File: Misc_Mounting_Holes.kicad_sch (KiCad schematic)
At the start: 15 parts

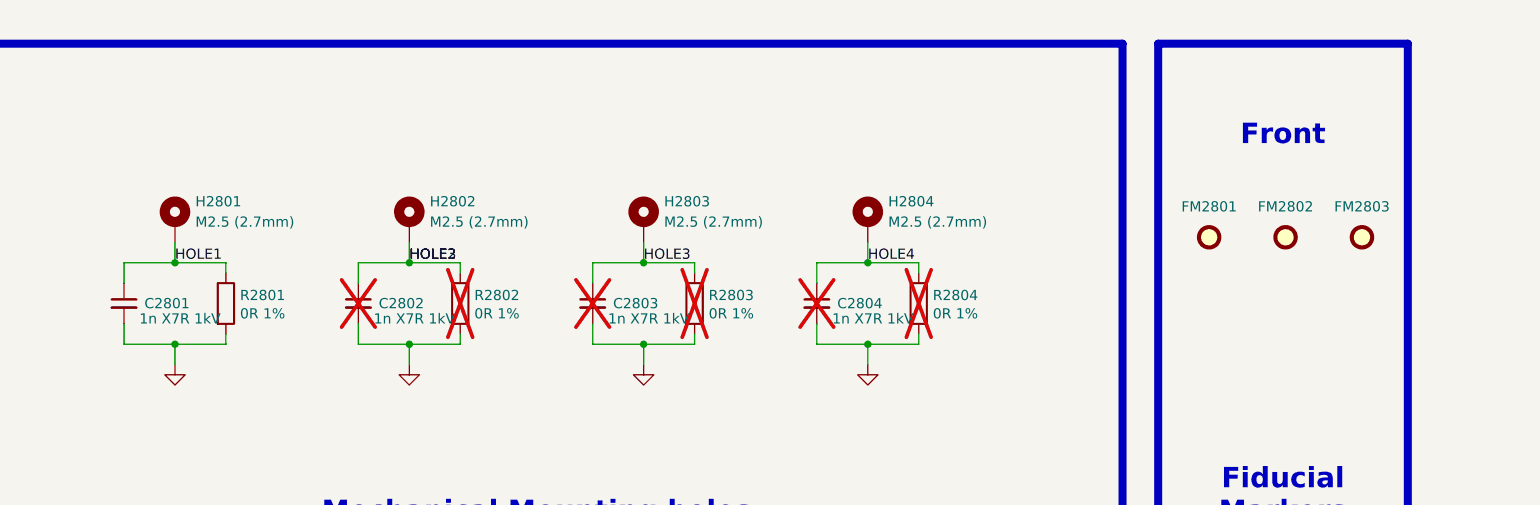
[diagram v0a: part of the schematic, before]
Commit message: Added RGB LED, added motor connectors, added test points, imported all 3D models
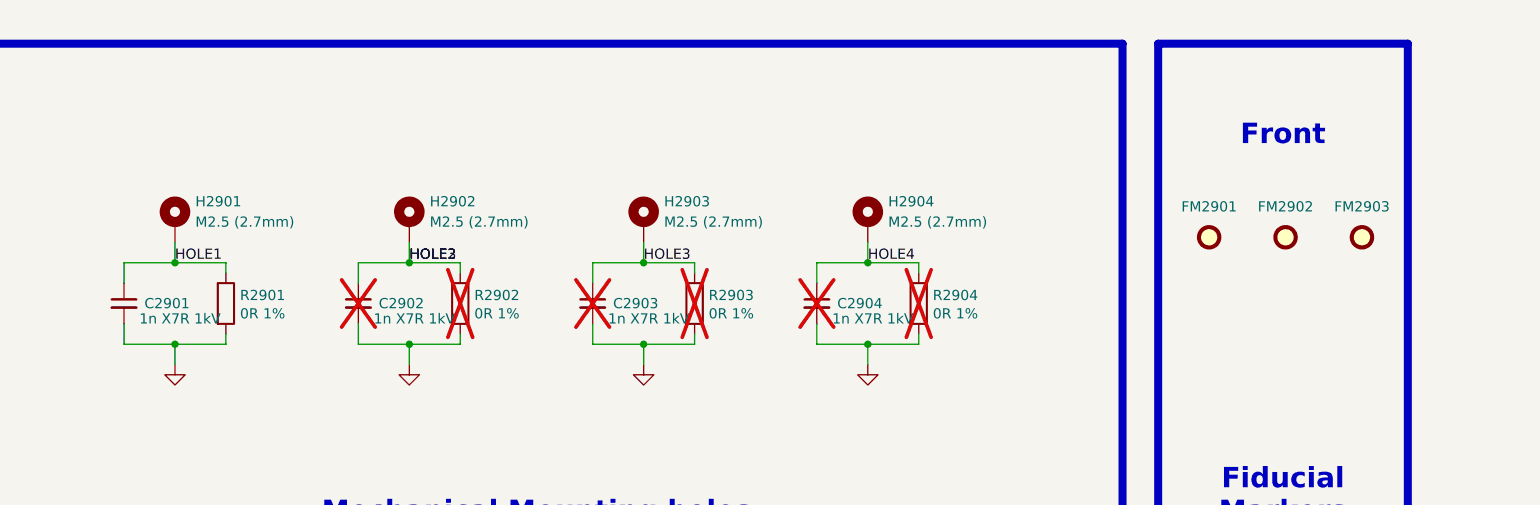
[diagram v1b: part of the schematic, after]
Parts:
- renumbered C2801 to C2901, C2802 to C2902, C2803 to C2903, C2804 to C2904, FM2801 to FM2901, FM2802 to FM2902, FM2803 to FM2903, H2801 to H2901, H2802 to H2902, H2803 to H2903, H2804 to H2904, R2801 to R2901, R2802 to R2902, R2803 to R2903, R2804 to R2904

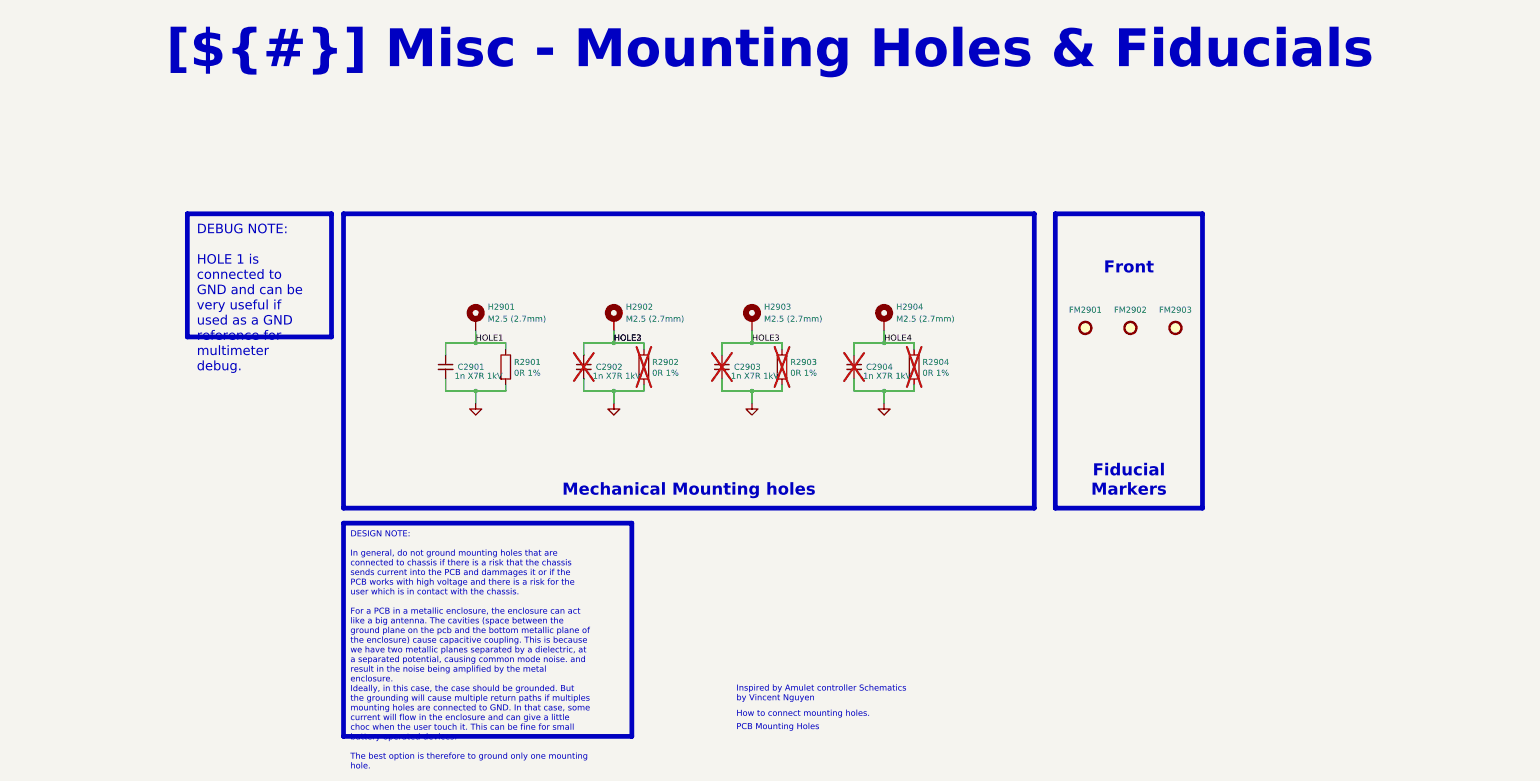
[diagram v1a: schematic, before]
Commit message: Finished schematic, imported all footprints, all 3D models and created STM32 project, now need to proofread shematic before layout
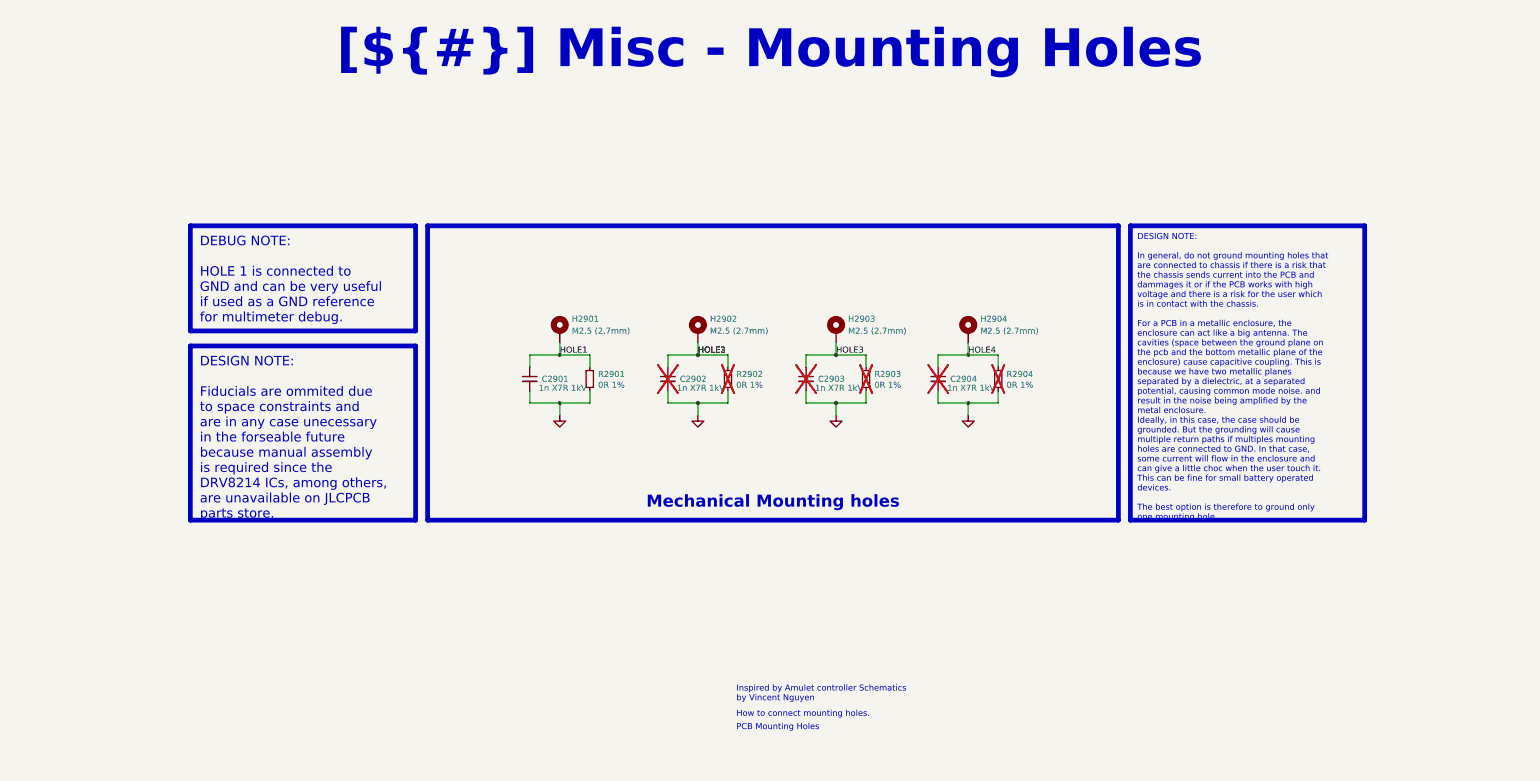
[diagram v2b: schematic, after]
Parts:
- removed FM2901, FM2902, FM2903: Fiducial, Charge_Manager_FP:Fiducial_1mm_Mask2mm, symbol Mechanical:Fiducial
- removed R2902, R2903, R2904: 0R 1%, Resistor_SMD:R_0603_1608Metric, symbol Device:R
- added R2902, R2903, R2904: 0R 1%, Resistor_SMD:R_0603_1608Metric, symbol Device:R_Small
- C2901, C2902, C2903, C2904: Manufacturer Part Number C0603C102MDRAC7081 -> C0603C102KDRACTU; Supplier Part Number 80-C0603C102MDRAC -> 80-C0603C102KDRACTU
- R2901: symbol Device:R -> Device:R_Small
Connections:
- net GND: now also R2902.2, R2903.2, R2904.2
- net HOLE2: now also R2902.1, R2903.1
- net HOLE4: now also R2904.1
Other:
- title: Misc - Mounting Holes & Fiducials -> Misc - Mounting Holes
- moved on the sheet: C2901, C2902, C2903, C2904, H2901, H2902, H2903, H2904, R2901

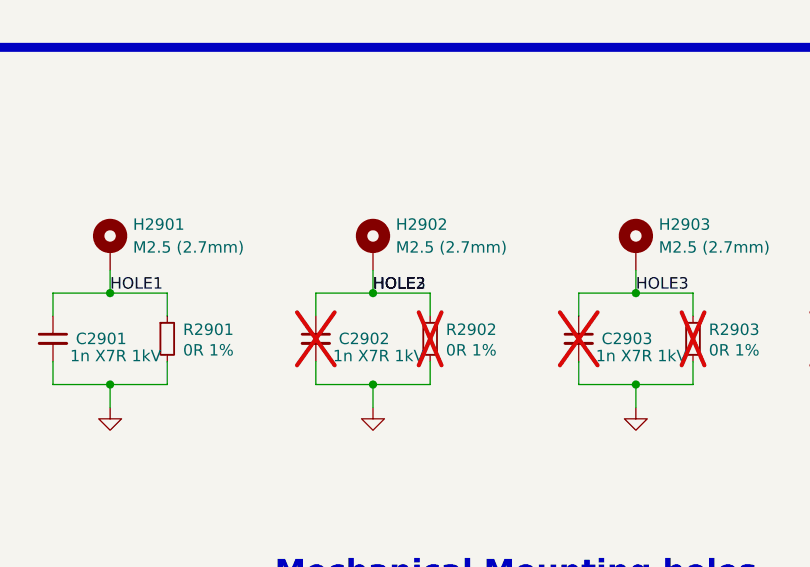
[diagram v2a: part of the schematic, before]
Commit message: Reviewed shematic, cleaned all DRC errors, chosed stackup, started layout
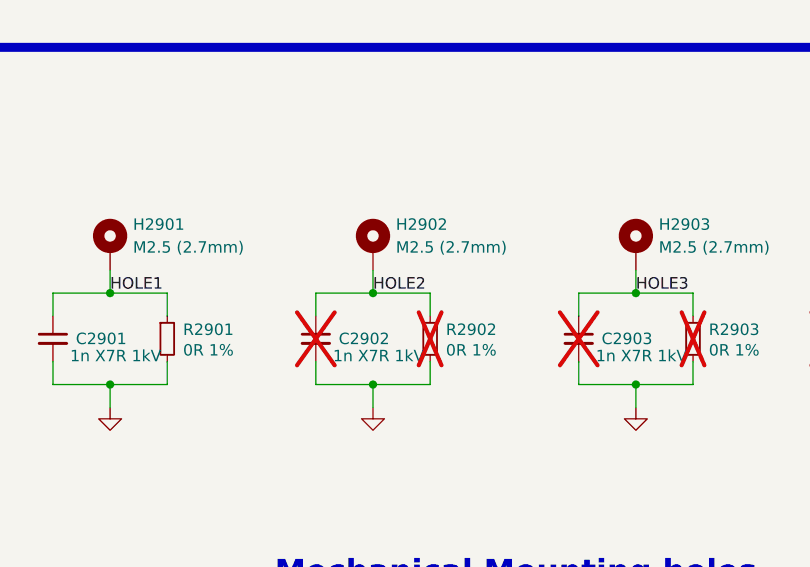
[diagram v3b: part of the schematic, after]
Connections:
- net HOLE2: no longer C2903.1, H2903.1, R2903.1
- new net HOLE3: C2903.1, H2903.1, R2903.1
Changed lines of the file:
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@@
-		)
-	)
-	(label "HOLE3"
-		(at 133.35 91.44 0)
-		(effects
-			(font
-				(size 1.27 1.27)
-			)
-			(justify left bottom)
 		)
 	)

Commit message: Finished layout, only cleaning left
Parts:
- C2901, R2901: now not fitted
- C2902, R2902: now fitted
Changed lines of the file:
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@@
 		(in_bom yes)
 		(on_board yes)
-		(dnp no)
+		(dnp yes)
 		(property "Reference" "C2901"
 			(at 100.33 96.52 0)
@@
 		(in_bom yes)
 		(on_board yes)
-		(dnp yes)
+		(dnp no)
 		(property "Reference" "R2902"
 			(at 144.272 95.504 0)
@@
 		(in_bom yes)
 		(on_board yes)
-		(dnp no)
+		(dnp yes)
 		(property "Reference" "R2901"
 			(at 115.062 95.504 0)
@@
 		(in_bom yes)
 		(on_board yes)
-		(dnp yes)
+		(dnp no)
 		(property "Reference" "C2902"
 			(at 129.54 96.52 0)

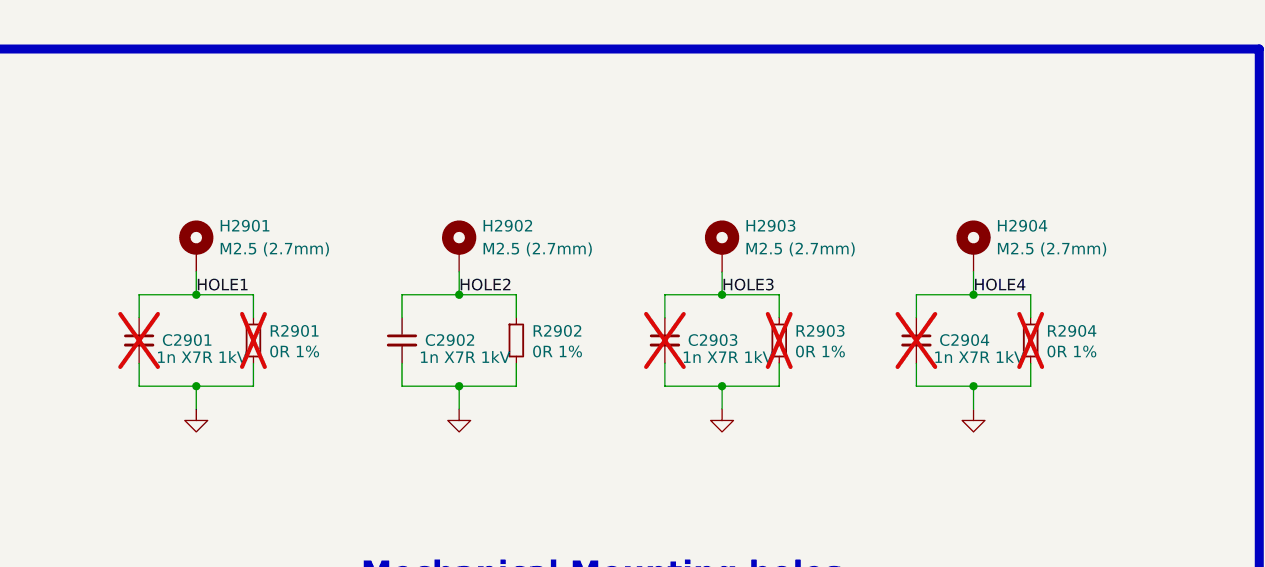
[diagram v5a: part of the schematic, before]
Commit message: Finished cleaning routing, removed errors, cleaned shematics, added pictures and other improvements
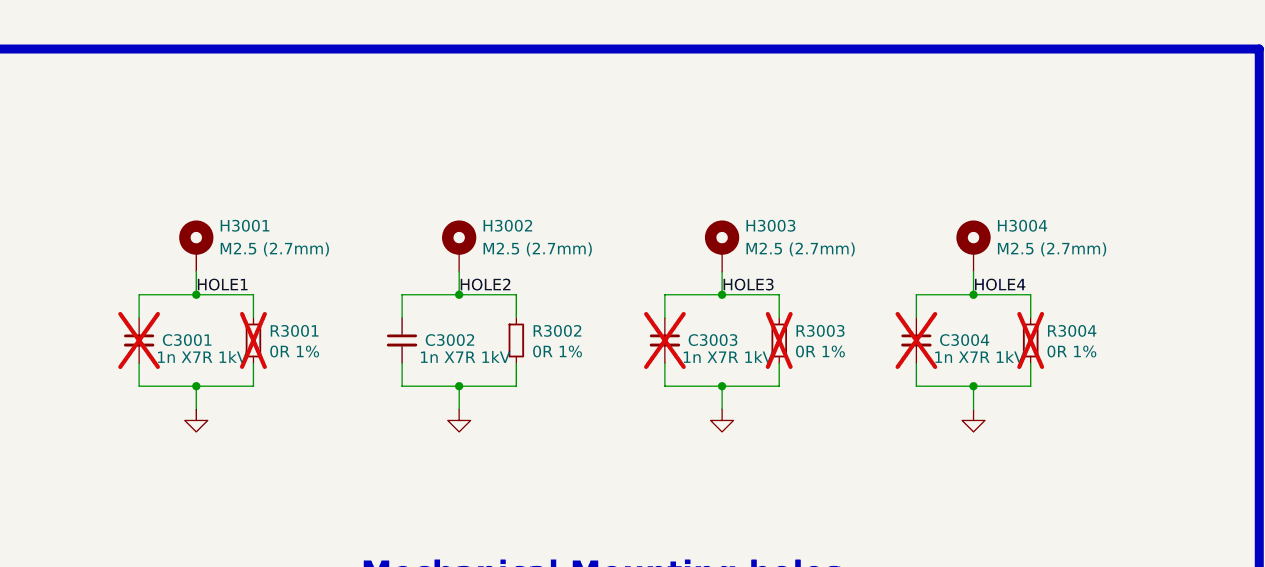
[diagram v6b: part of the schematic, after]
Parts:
- renumbered C2901 to C3001, C2902 to C3002, C2903 to C3003, C2904 to C3004, H2901 to H3001, H2902 to H3002, H2903 to H3003, H2904 to H3004, R2901 to R3001, R2902 to R3002, R2903 to R3003, R2904 to R3004
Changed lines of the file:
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@@
 		(on_board yes)
 		(dnp yes)
-		(property "Reference" "R2903"
+		(property "Reference" "R3003"
 			(at 173.482 95.504 0)
 			(effects
@@
 			(project "Plume"
 				(path "/0650c7a8-acba-429c-9f8e-eec0baf0bc1c/fede4c36-00cc-4d3d-b71c-5243ba232202/93c115ca-2823-4ddf-b830-32015e2ac9e9"
-					(reference "R2903")
+					(reference "R3003")
 					(unit 1)
 				)
@@
 		(on_board yes)
 		(dnp yes)
-		(property "Reference" "C2901"
+		(property "Reference" "C3001"
 			(at 100.33 96.52 0)
 			(effects
@@
 			(project "Plume"
 				(path "/0650c7a8-acba-429c-9f8e-eec0baf0bc1c/fede4c36-00cc-4d3d-b71c-5243ba232202/93c115ca-2823-4ddf-b830-32015e2ac9e9"
-					(reference "C2901")
+					(reference "C3001")
 					(unit 1)
 				)
@@
 		(on_board yes)
 		(dnp no)
-		(property "Reference" "R2902"
+		(property "Reference" "R3002"
 			(at 144.272 95.504 0)
 			(effects
@@
 			(project "Plume"
 				(path "/0650c7a8-acba-429c-9f8e-eec0baf0bc1c/fede4c36-00cc-4d3d-b71c-5243ba232202/93c115ca-2823-4ddf-b830-32015e2ac9e9"
-					(reference "R2902")
+					(reference "R3002")
 					(unit 1)
 				)
@@
 		(dnp no)
 		(fields_autoplaced yes)
-		(property "Reference" "H2901"
+		(property "Reference" "H3001"
 			(at 106.68 83.82 0)
 			(effects
@@
 			(project "Plume"
 				(path "/0650c7a8-acba-429c-9f8e-eec0baf0bc1c/fede4c36-00cc-4d3d-b71c-5243ba232202/93c115ca-2823-4ddf-b830-32015e2ac9e9"
-					(reference "H2901")
+					(reference "H3001")
 					(unit 1)
 				)
@@
 		(dnp no)
 		(fields_autoplaced yes)
-		(property "Reference" "H2902"
+		(property "Reference" "H3002"
 			(at 135.89 83.82 0)
 			(effects
@@
 			(project "Plume"
 				(path "/0650c7a8-acba-429c-9f8e-eec0baf0bc1c/fede4c36-00cc-4d3d-b71c-5243ba232202/93c115ca-2823-4ddf-b830-32015e2ac9e9"
-					(reference "H2902")
+					(reference "H3002")
 					(unit 1)
 				)
@@
 		(on_board yes)
 		(dnp yes)
-		(property "Reference" "C2904"
+		(property "Reference" "C3004"
 			(at 186.69 96.52 0)
 			(effects
@@
 			(project "Plume"
 				(path "/0650c7a8-acba-429c-9f8e-eec0baf0bc1c/fede4c36-00cc-4d3d-b71c-5243ba232202/93c115ca-2823-4ddf-b830-32015e2ac9e9"
-					(reference "C2904")
+					(reference "C3004")
 					(unit 1)
 				)
@@
 		(dnp no)
 		(fields_autoplaced yes)
-		(property "Reference" "H2903"
+		(property "Reference" "H3003"
 			(at 165.1 83.82 0)
 			(effects
@@
 			(project "Plume"
 				(path "/0650c7a8-acba-429c-9f8e-eec0baf0bc1c/fede4c36-00cc-4d3d-b71c-5243ba232202/93c115ca-2823-4ddf-b830-32015e2ac9e9"
-					(reference "H2903")
+					(reference "H3003")
 					(unit 1)
 				)
@@
 		(dnp no)
 		(fields_autoplaced yes)
-		(property "Reference" "#PWR02903"
+		(property "Reference" "#PWR03003"
 			(at 162.56 110.49 0)
 			(effects
@@
 			(project "Plume"
 				(path "/0650c7a8-acba-429c-9f8e-eec0baf0bc1c/fede4c36-00cc-4d3d-b71c-5243ba232202/93c115ca-2823-4ddf-b830-32015e2ac9e9"
-					(reference "#PWR02903")
+					(reference "#PWR03003")
 					(unit 1)
 				)
@@
 		(dnp no)
 		(fields_autoplaced yes)
-		(property "Reference" "H2904"
+		(property "Reference" "H3004"
 			(at 193.04 83.82 0)
 			(effects
@@
 			(project "Plume"
 				(path "/0650c7a8-acba-429c-9f8e-eec0baf0bc1c/fede4c36-00cc-4d3d-b71c-5243ba232202/93c115ca-2823-4ddf-b830-32015e2ac9e9"
-					(reference "H2904")
+					(reference "H3004")
 					(unit 1)
 				)
@@
 		(on_board yes)
 		(dnp yes)
-		(property "Reference" "R2904"
+		(property "Reference" "R3004"
 			(at 201.422 95.504 0)
 			(effects
@@
 			(project "Plume"
 				(path "/0650c7a8-acba-429c-9f8e-eec0baf0bc1c/fede4c36-00cc-4d3d-b71c-5243ba232202/93c115ca-2823-4ddf-b830-32015e2ac9e9"
-					(reference "R2904")
+					(reference "R3004")
 					(unit 1)
 				)
@@
 		(on_board yes)
 		(dnp yes)
-		(property "Reference" "R2901"
+		(property "Reference" "R3001"
 			(at 115.062 95.504 0)
 			(effects
@@
 			(project "Plume"
 				(path "/0650c7a8-acba-429c-9f8e-eec0baf0bc1c/fede4c36-00cc-4d3d-b71c-5243ba232202/93c115ca-2823-4ddf-b830-32015e2ac9e9"
-					(reference "R2901")
+					(reference "R3001")
 					(unit 1)
 				)
@@
 		(dnp no)
 		(fields_autoplaced yes)
-		(property "Reference" "#PWR02901"
+		(property "Reference" "#PWR03001"
 			(at 104.14 110.49 0)
 			(effects
@@
 			(project "Plume"
 				(path "/0650c7a8-acba-429c-9f8e-eec0baf0bc1c/fede4c36-00cc-4d3d-b71c-5243ba232202/93c115ca-2823-4ddf-b830-32015e2ac9e9"
-					(reference "#PWR02901")
+					(reference "#PWR03001")
 					(unit 1)
 				)
@@
 		(dnp no)
 		(fields_autoplaced yes)
-		(property "Reference" "#PWR02904"
+		(property "Reference" "#PWR03004"
 			(at 190.5 110.49 0)
 			(effects
@@
 			(project "Plume"
 				(path "/0650c7a8-acba-429c-9f8e-eec0baf0bc1c/fede4c36-00cc-4d3d-b71c-5243ba232202/93c115ca-2823-4ddf-b830-32015e2ac9e9"
-					(reference "#PWR02904")
+					(reference "#PWR03004")
 					(unit 1)
 				)
@@
 		(on_board yes)
 		(dnp yes)
-		(property "Reference" "C2903"
+		(property "Reference" "C3003"
 			(at 158.75 96.52 0)
 			(effects
@@
 			(project "Plume"
 				(path "/0650c7a8-acba-429c-9f8e-eec0baf0bc1c/fede4c36-00cc-4d3d-b71c-5243ba232202/93c115ca-2823-4ddf-b830-32015e2ac9e9"
-					(reference "C2903")
+					(reference "C3003")
 					(unit 1)
 				)
@@
 		(on_board yes)
 		(dnp no)
-		(property "Reference" "C2902"
+		(property "Reference" "C3002"
 			(at 129.54 96.52 0)
 			(effects
@@
 			(project "Plume"
 				(path "/0650c7a8-acba-429c-9f8e-eec0baf0bc1c/fede4c36-00cc-4d3d-b71c-5243ba232202/93c115ca-2823-4ddf-b830-32015e2ac9e9"
-					(reference "C2902")
+					(reference "C3002")
 					(unit 1)
 				)
@@
 		(dnp no)
 		(fields_autoplaced yes)
-		(property "Reference" "#PWR02902"
+		(property "Reference" "#PWR03002"
 			(at 133.35 110.49 0)
 			(effects
@@
 			(project "Plume"
 				(path "/0650c7a8-acba-429c-9f8e-eec0baf0bc1c/fede4c36-00cc-4d3d-b71c-5243ba232202/93c115ca-2823-4ddf-b830-32015e2ac9e9"
-					(reference "#PWR02902")
-					(unit 1)
-				)
+					(reference "#PWR03002")
+					(unit 1)
+				)
